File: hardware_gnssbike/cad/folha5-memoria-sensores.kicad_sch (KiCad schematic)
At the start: 16 parts, among them U501 MX25R6435F, U502 Bosch BMP585, U503 Bosch BMI270, U504 MMC5633NJL, U505 TI OPT3001DNPR

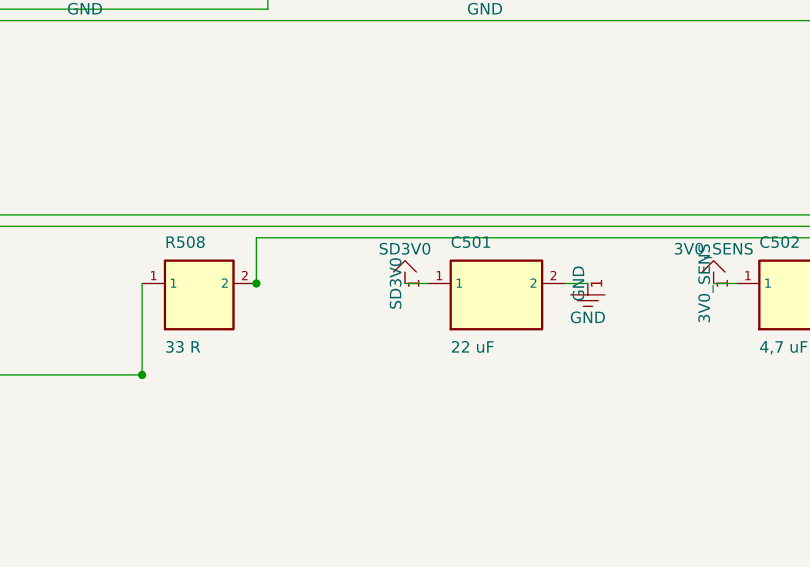
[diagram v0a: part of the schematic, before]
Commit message: fix(hardware): fail the schematic check when a pin sits in two nets
A pin in two nets is a short, and the check merged the two nets instead of
complaining: U103's SDA was in both PWR_SDA and the 3V0 rail, which tied the
whole power bus to 3.0 V and shorted out R107, and the merge hid it. Now any
pin in two nets fails, except for the connectors declared in PASSA_DIRETO,
where a connector and the part behind it really are one node drawn as two.

Three more things the check then caught, all in the energy sheet:

  - the AEM10900's inductor had one end on a net of its own going nowhere.
    It boosts 1.67 V to 3.9 V, so the far end belongs on SRC; the open item
    now says to confirm it against figure 3 of DS-AEM10900-v1.6.0.
  - the flash's 22 uF bulk sat before the current jumper instead of beside
    the part, which is what 02-calculos.md asks for and what every other
    block on this board does.
  - four decoupling capacitors had no ground.

The unconnected pins are now written out one by one with the reason, so a
loose end is a decision on the page and not an absence.
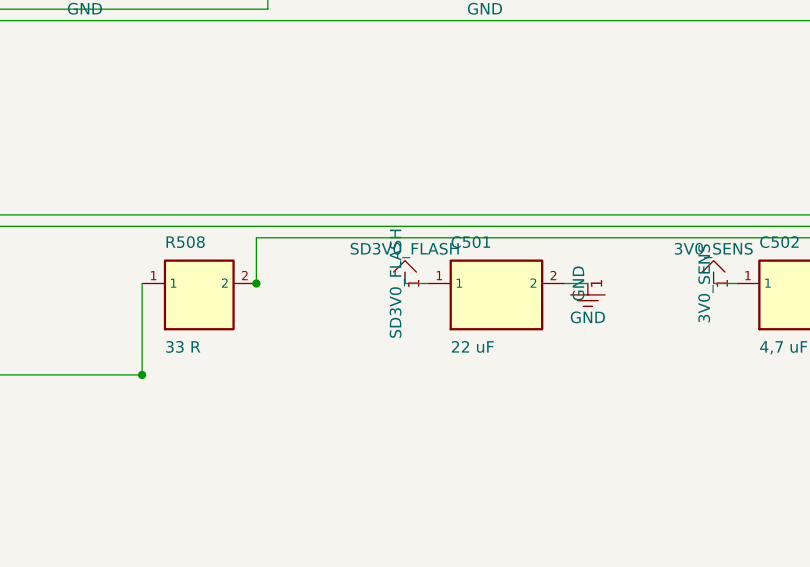
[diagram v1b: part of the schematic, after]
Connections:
- net SD3V0: no longer C501.1
- net SD3V0_FLASH: now also C501.1
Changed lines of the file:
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@@
+	(wire
+		(pts
+			(xy 270.510 31.750) (xy 270.510 29.210)
+		)
+		(stroke (width 0) (type default))
+	)
 	(wire
 		(pts
 			(xy 156.210 83.820) (xy 153.670 83.820)
-		)
-		(stroke (width 0) (type default))
-	)
-	(wire
-		(pts
-			(xy 270.510 31.750) (xy 270.510 29.210)
 		)
 		(stroke (width 0) (type default))
@@
 	)
 	(symbol
-		(lib_id "power:SD3V0")
-		(at 153.670 83.820 0)
-		(unit 1)
-		(exclude_from_sim no)
-		(in_bom no)
-		(on_board yes)
-		(dnp no)
-		(property "Reference" "#PWR030"
-			(at 153.67000000000002 83.82 0)
-			(effects (font (size 1.27 1.27)) (hide yes))
-		)
-		(property "Value" "SD3V0"
-			(at 153.670 80.010 0)
-			(effects (font (size 1.27 1.27)))
-		)
-		(property "Footprint" ""
-			(at 153.67000000000002 83.82 0)
-			(effects (font (size 1.27 1.27)) (hide yes))
-		)
-		(property "Datasheet" ""
-			(at 153.67000000000002 83.82 0)
-			(effects (font (size 1.27 1.27)) (hide yes))
-		)
-		(pin "1")
-		(instances
-			(project "gnssbike"
-				(path "/9c874366-f223-4aef-8b18-3e2a2bab2b25/613acabb-6b32-418f-89ed-a184dc396d24"
-					(reference "#PWR030")
-					(unit 1)
-				)
-			)
-		)
-	)
-	(symbol
 		(lib_id "power:SD3V0_FLASH")
 		(at 270.510 29.210 0)
@@
 		(on_board yes)
 		(dnp no)
-		(property "Reference" "#PWR031"
+		(property "Reference" "#PWR030"
 			(at 270.51 29.21 0)
 			(effects (font (size 1.27 1.27)) (hide yes))
@@
 			(effects (font (size 1.27 1.27)) (hide yes))
 		)
+		(pin "1")
+		(instances
+			(project "gnssbike"
+				(path "/9c874366-f223-4aef-8b18-3e2a2bab2b25/613acabb-6b32-418f-89ed-a184dc396d24"
+					(reference "#PWR030")
+					(unit 1)
+				)
+			)
+		)
+	)
+	(symbol
+		(lib_id "power:SD3V0_FLASH")
+		(at 153.670 83.820 0)
+		(unit 1)
+		(exclude_from_sim no)
+		(in_bom no)
+		(on_board yes)
+		(dnp no)
+		(property "Reference" "#PWR031"
+			(at 153.67000000000002 83.82 0)
+			(effects (font (size 1.27 1.27)) (hide yes))
+		)
+		(property "Value" "SD3V0_FLASH"
+			(at 153.670 80.010 0)
+			(effects (font (size 1.27 1.27)))
+		)
+		(property "Footprint" ""
+			(at 153.67000000000002 83.82 0)
+			(effects (font (size 1.27 1.27)) (hide yes))
+		)
+		(property "Datasheet" ""
+			(at 153.67000000000002 83.82 0)
+			(effects (font (size 1.27 1.27)) (hide yes))
+		)

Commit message: feat(hardware): the test points, a readable silkscreen, and paper that fits
Eleven of the sixteen test points of 06-conectores-e-pontos-de-teste.md were
not on the board. Only the three of the console sheet existed; a rail you
cannot put a probe on is a rail you cannot debug. VBUS, VBUSOUT, VBAT, VSYS,
3V0, 1V8, SD3V0, 3V3BL, VBCKP, VINT and the ground reference are there now,
each beside the thing it measures, and each takes what is LEFT: placed with
the rest of JUNTO they pushed three decoupling capacitors off their rings,
one of them to 4.0 mm from a pin that wants 2. The two that are still
missing are the document's own absences - TP111 measures ST_STO, which the
AEM10900 datasheet does not have, and TP401 measures 5V0, from a regulator
not fitted with the JDI panel. The list lives in parts.TESTE and nets.py
refuses a point that names a net that does not exist.

The silkscreen named nothing. Every reference sat 1.8 mm above its part at
0.7 mm with a 0.1 mm stroke - below the floor every fab publishes - and 37
pairs of designators printed on top of each other. The text is at the fab
minimum now, 0.8 mm with 0.15, and each label is PLACED: candidates around
its own courtyard, nearest first, never over another label and preferably
not over another part's outline. 127 references, 0 overlapping. The mounting
hole's REF** is hidden; it names nothing and was the last label sitting on
another.

Ground: a mesh, not just a hem. Edge stitching keeps the boundary of the
surface pours from becoming a radiating slot and does nothing for the
middle, where a patch of pour that reaches the inner plane through a via
20 mm away is not ground at 2.4 GHz. A 4.0 mm grid of ground vias now
covers the board - under the 6.1 mm that is a tenth of a wavelength in
FR-4 - laid last, on what is free, so a stitch never costs a connection.

The router's search learned about pad fields. The neck beside a pad existed
only in emitir(), and emitir only ever sees paths the search already found,
so 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
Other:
- moved on the sheet: C501, C502, C503, R501, R502, R503, R504, R505, R506, R507, R508, U501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

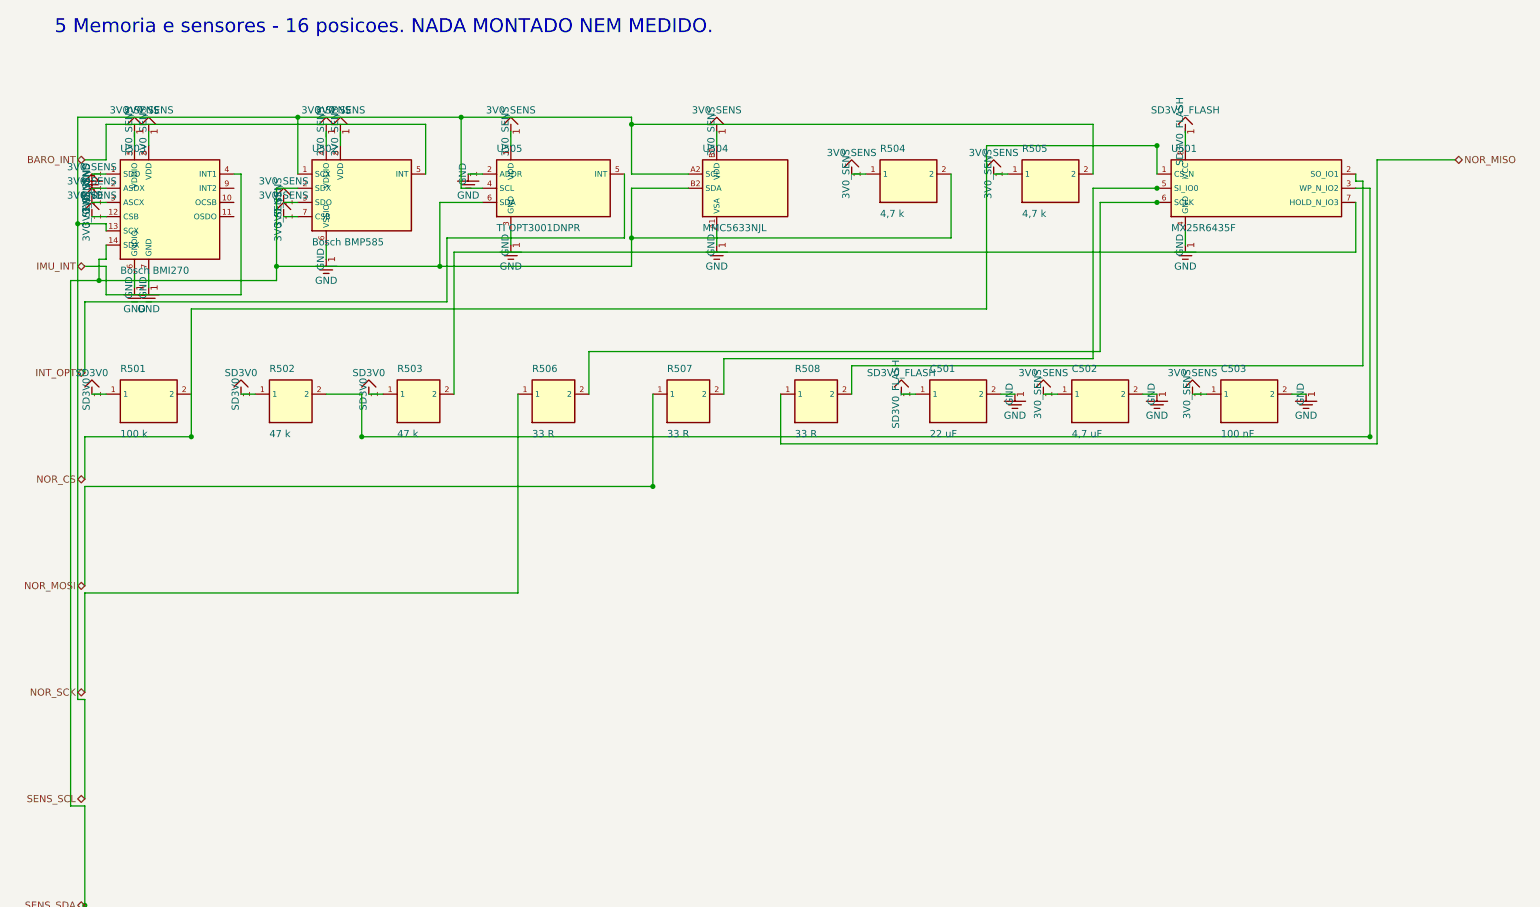
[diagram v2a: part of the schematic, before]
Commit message: feat(hardware): draw each part as its own symbol, not as a block
A rectangle with pin names down its sides is how an INTEGRATED CIRCUIT is
drawn, and only an integrated circuit. This generator drew all 127 parts
that way - resistors, ceramic capacitors, diodes, the TVS - and a sheet of
blocks joined by lines does not show a circuit.

Every class has its own symbol now, in the standard form, with the lead
axis on x and the body between -1.27 and +1.27 mm: a zigzag for a resistor
and a 0 ohm link (42 of them), two parallel plates for a ceramic capacitor
and a curved plate with a + for an electrolytic (31), four arcs for an
inductor (4), the same arcs inside a rectangle for a ferrite bead, which is
what tells the two apart, a zigzag with a diagonal arrow for the thermistor,
a triangle and a bar for a diode with arrows leaving it for an LED, two
contacts with a bar and a plunger for a key, a circle with a diagonal for
the buzzer, and a circle on the end of a lead for a test point. The 36 that
stay rectangles are the ones that should be: the ICs, the connectors and the
display. A two terminal part no longer prints pin numbers or pin names -
"1" and "2" on a resistor is noise, and the symbol already says which end is
which where it matters.

The power symbols had room reserved for the symbol and none for its NAME:
two ground pins two grid steps apart each got their own symbol, the symbols
did not collide, and the words printed over each other - "GNDGNDGND" along
the bottom of every chip. What is reserved now is the whole thing. With a
limit: the first cut let the stub run to fourteen grid steps looking for a
clear spot, and one of them crossed a component and split a net. A long stub
is worse than a crowded label, so it stops at eight and the label gives way.

One attempt is NOT in this commit, on purpose. Grouping every pin of a rail
on one edge into a single symbol - which is what a person draws - joins the
stubs with a line that runs along the part's edge and crosses w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
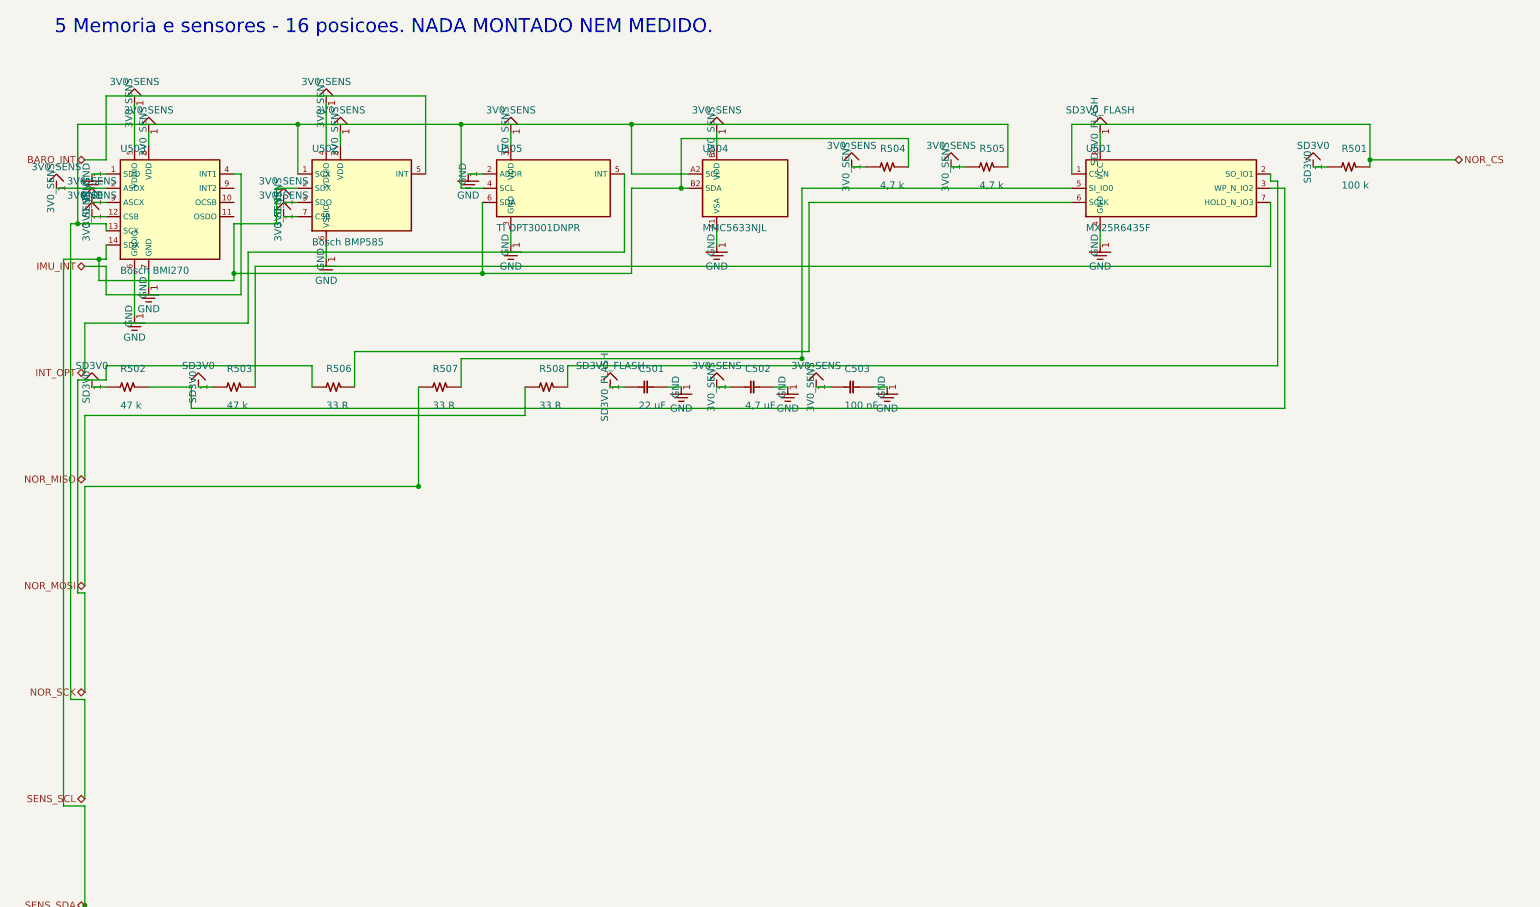
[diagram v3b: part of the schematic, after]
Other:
- moved on the sheet: U501

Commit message: feat(hardware): buy what JLCPCB can actually assemble
The board is made and assembled at JLCPCB, so every part has to be one
LCSC stocks - the owner's rule of 2026-09-24, with the Minew module and
the solar cells as the only exceptions. Three surveys against LCSC's
catalogue and JLCPCB's assembly API checked the 34 parts that are not a
plain resistor or capacitor, and this is what came back.

Parts that changed, and what each change costs:

  J101  Molex 2036150003 -> HRO TYPE-C-31-M-12 (C165948). 309 in the
        world at US$ 5,69 against 91.943 at US$ 0,186, and KiCad carries
        the land pattern under the part's own name. The body goes from
        8,58 to 7,35 mm, so the case opening changes.
  D101  ESD761DPYR -> TPD1E05U06DPYR (C436349). Same X1SON-2 and better
        capacitance, but bidirectional 24 V becomes unidirectional
        5,5 V: orientation now matters and a faulty cable putting 20 V
        on a CC line is no longer survivable.
  J103  three pairs of spring pads -> one JST ZH of 4 ways, with three
        0 ohm joining the groups to SRC. Nobody assembles a spring, a
        bicycle vibrates, and a pressed contact that opens and closes on
        the input of a switching converter is a dirty transient. ZH of
        1,5 mm on purpose: the cell is a GH of 1,25 and 4,2 V into the
        harvester's 2,73 V input would kill it. The 0 ohm let one face
        be measured alone in the sun.
  D105  new: a clamp on SRC. The right connector stops the mistake; the
        clamp stops the damage when the mistake comes from a crimp.
  J101  the shell had no pin, so four pads of the land pattern floated.

U101 and U103 stay as they are and go by consignment: the nPM1300 QFN is
zero on both sides and the whole e-peas line is zero. The nPM1300 does
exist in WLCSP-35, but its 0,419 x 0,440 mm ball pitch is smaller than
this board's 0,45 mm via and would force via-in-pad on every board ever
made, probably six layers, twice the thermal resistance and a light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
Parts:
- U501: footprint Package_SO:SOIC-8_5.23x5.23mm_P1.27mm -> Package_SO:SOIC-8_5.275x5.275mm_P1.27mm
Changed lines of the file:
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@@
 			(effects (font (size 1.27 1.27)) (justify left top))
 		)
-		(property "Footprint" "Package_SO:SOIC-8_5.23x5.23mm_P1.27mm"
+		(property "Footprint" "Package_SO:SOIC-8_5.275x5.275mm_P1.27mm"
 			(at 219.71 39.37 0)
 			(effects (font (size 1.27 1.27)) (hide yes))

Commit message: feat(hardware): the four parts LCSC forced out, drawn from their drawings
The switch, the buzzer, the RGB LED and the magnetometer all had to
change, and each one came back from its drawing with something the
catalogue does not say.

  SW601..603  Omron B3S-1002P -> XunPu TS-1088R-02026 (C455280). It has
        TWO terminals, not four, so the land pattern is new even though
        the schematic already treated the key as two ends. Body 3,90 x
        3,00 x 2,00 against 6,6 x 6 x 3,4, which frees half the area the
        three keys took on the edge, and 260 gf against 230 - firmer,
        which is what gloves want. But the plunger rises only 0,50 mm
        above the steel cap against the Omron's 0,7, and the keys are
        pressed through the case: the case plunger changes.

  LS601  Same Sky CPT-1117-83-SMT (ONE in stock) -> Murata
        PKLCS1212E4001-R1 (C113159), the only substitute that keeps the
        84 dB. At 25 km/h with wind, the 65 to 70 dB of the 9 x 9 parts
        is inaudible, and an inaudible buzzer is no buzzer. The drawing
        corrects two things the catalogue hides: the sound hole is a
        LATERAL slot of 1,9 x 0,9 mm whose lower edge sits 0,30 mm off
        the board, with a channel underneath leaving by the opposite
        wall - so the case needs a side duct, not a hole in the lid -
        and the body is uniform dark graphite, with gold terminals, not
        black with a pale top. It also asks for 1 k to 2 k in series and
        forbids DC, which R607 and R608 now have to be checked against.

  D601  Kingbright APTF1616 (the suffix no longer exists, and what does
        has 305 pieces) -> TUOZHAN S4-3528RGBTA-A (C2827321), 2 million
        in stock at a twentieth of the price, common anode as the design
        wants. It is 3,5 x 2,8 instead of 1,6 x 1,6, so the LED zone had
        to widen and the part moved down 0,6 mm: at 1,9 mm tall it stood
        3,25 mm from the light sensor, which asks for twice a
        ne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
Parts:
- U504: value MMC5633NJL -> Memsic MMC5603NJ; footprint gnssbike:MMC5633_WLP-4_0.85x0.85mm -> gnssbike:MMC5603_WLP-4_0.82x0.82mm
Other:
- moved on the sheet: R501, R504, R505, U501, U504
